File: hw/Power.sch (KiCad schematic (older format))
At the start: 32 parts, among them J201 Conn_01x02, Q201 AO3401A, Q202 AO3401A, Q203 IRLML6344TRPBF, Q204 IRLML6344TRPBF, U201 AP1501-K5, U202 RT6200

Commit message: Updates to board revision 0.2 and newer HAL version
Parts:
- removed Q201, Q202: AO3401A, digikey-footprints:SOT-23-3, symbol dk_Transistors-FETs-MOSFETs-Single:AO3401A
- removed Q203, Q204: IRLML6344TRPBF, digikey-footprints:SOT-23-3, symbol dk_Transistors-FETs-MOSFETs-Single:IRLML6344TRPBF
- removed R209, R210, R212, R214: 100k, Resistors_SMD:R_0603_HandSoldering, symbol Device:R_Small
- removed R211, R213: 10k, Resistors_SMD:R_0603_HandSoldering, symbol Device:R_Small
- U201: symbol Misc:AP1501-K5 -> Telemetry-rescue:AP1501-K5-Misc
- U202: symbol Misc:RT6200 -> Telemetry-rescue:RT6200-Misc
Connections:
- net labels removed: VBUS
- wire segments 114 -> 73

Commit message: Pin remapping and layout improvements
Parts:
- added C207, C212: 100n, Capacitor_SMD:C_0805_2012Metric_Pad1.15x1.40mm_HandSolder, symbol Device:C
- added C209, C210: 10n, Capacitor_SMD:C_0805_2012Metric_Pad1.15x1.40mm_HandSolder, symbol Device:C
- added C211: 100n, Capacitor_SMD:C_0805_2012Metric_Pad1.15x1.40mm_HandSolder, symbol Device:C_Small
- C201: value 22u -> 470uF/35V; footprint Capacitors_ThroughHole:C_Radial_D7.5_L11.2_P2.5 -> Capacitor_THT:CP_Radial_D10.0mm_P5.00mm
- C202, C208: value 22u -> 100uF/10V
- C203: footprint Capacitors_SMD:C_0603_HandSoldering -> Capacitor_SMD:C_0603_1608Metric_Pad1.05x0.95mm_HandSolder
- C205, C206: footprint Capacitors_SMD:C_0805 -> Capacitor_SMD:C_0805_2012Metric_Pad1.15x1.40mm_HandSolder
- R201: footprint Resistors_SMD:R_0603_HandSoldering -> Resistor_SMD:R_0603_1608Metric_Pad1.05x0.95mm_HandSolder; symbol Device:R -> Device:R_Small
- R202, R203, R204, R205, R206, R207, R208: footprint Resistors_SMD:R_0603_HandSoldering -> Resistor_SMD:R_0603_1608Metric_Pad1.05x0.95mm_HandSolder
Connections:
- net +BATT: now also C207.1, C209.1, C210.1; no longer R201.2
- net GND: now also R201.2, C207.2, C209.2, C212.2
- net VCC: now also C211.1, C212.1
- net at R202.2, R204.1, U201.4 (FB): now also C211.2
- net at R201.1, U201.5 (~SD): now also C210.2
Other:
- moved on the sheet: C202, C208, D202, L202, R201, R202, R204, U201

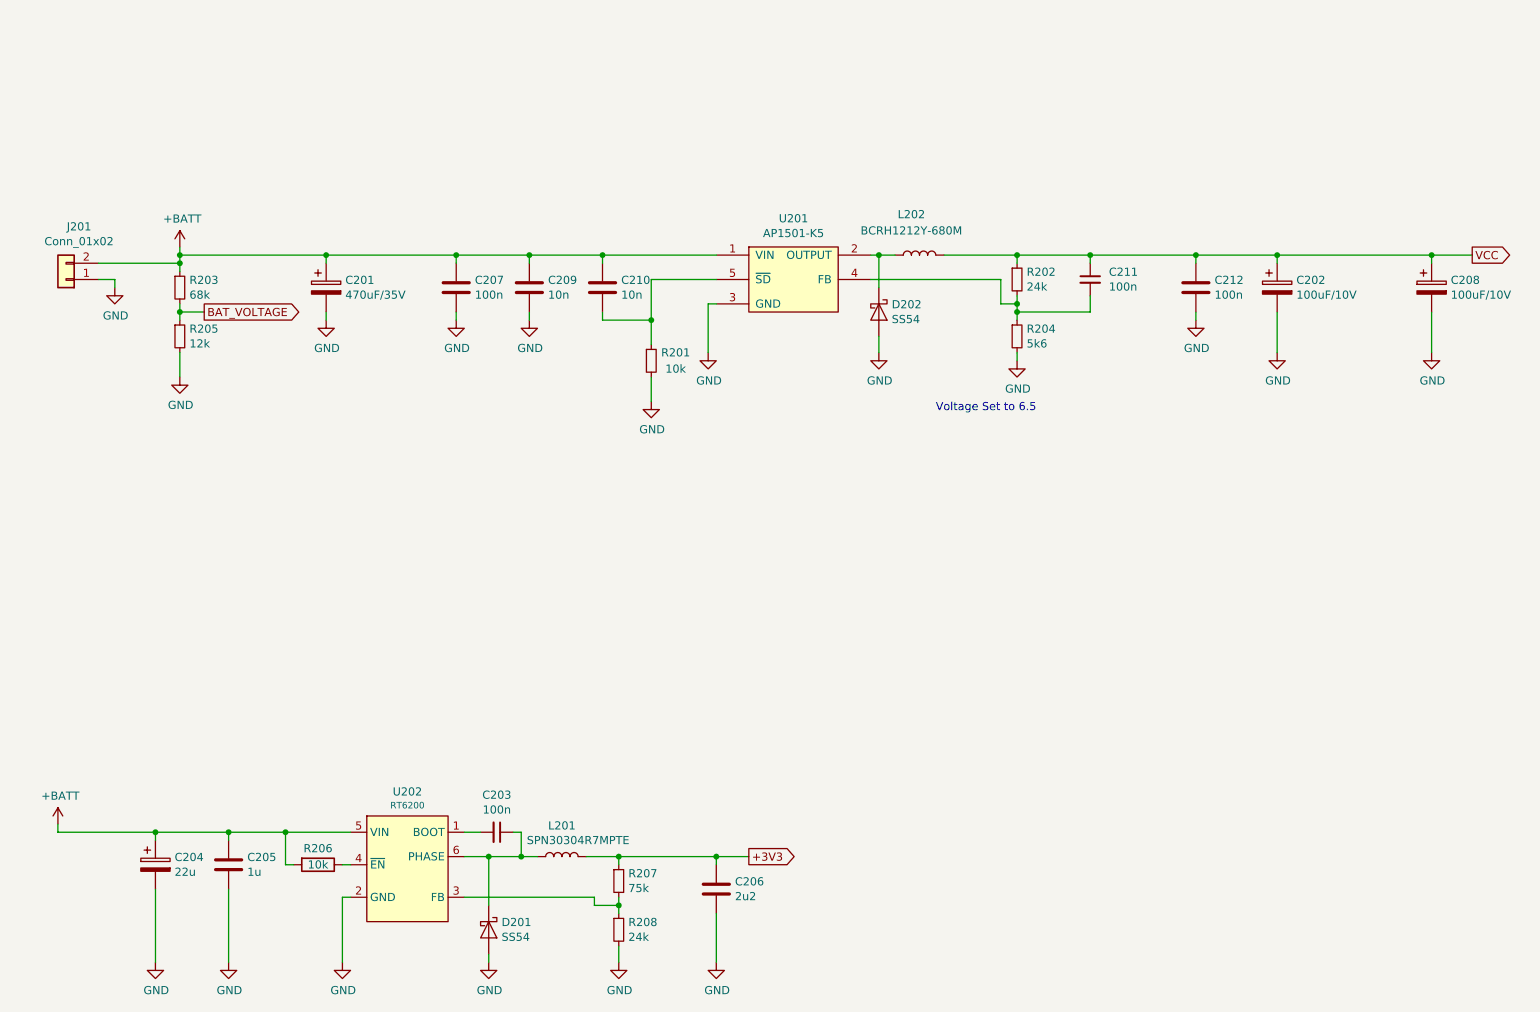
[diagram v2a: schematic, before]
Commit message: Changed High current pwm connectors to 5mm pitch versions
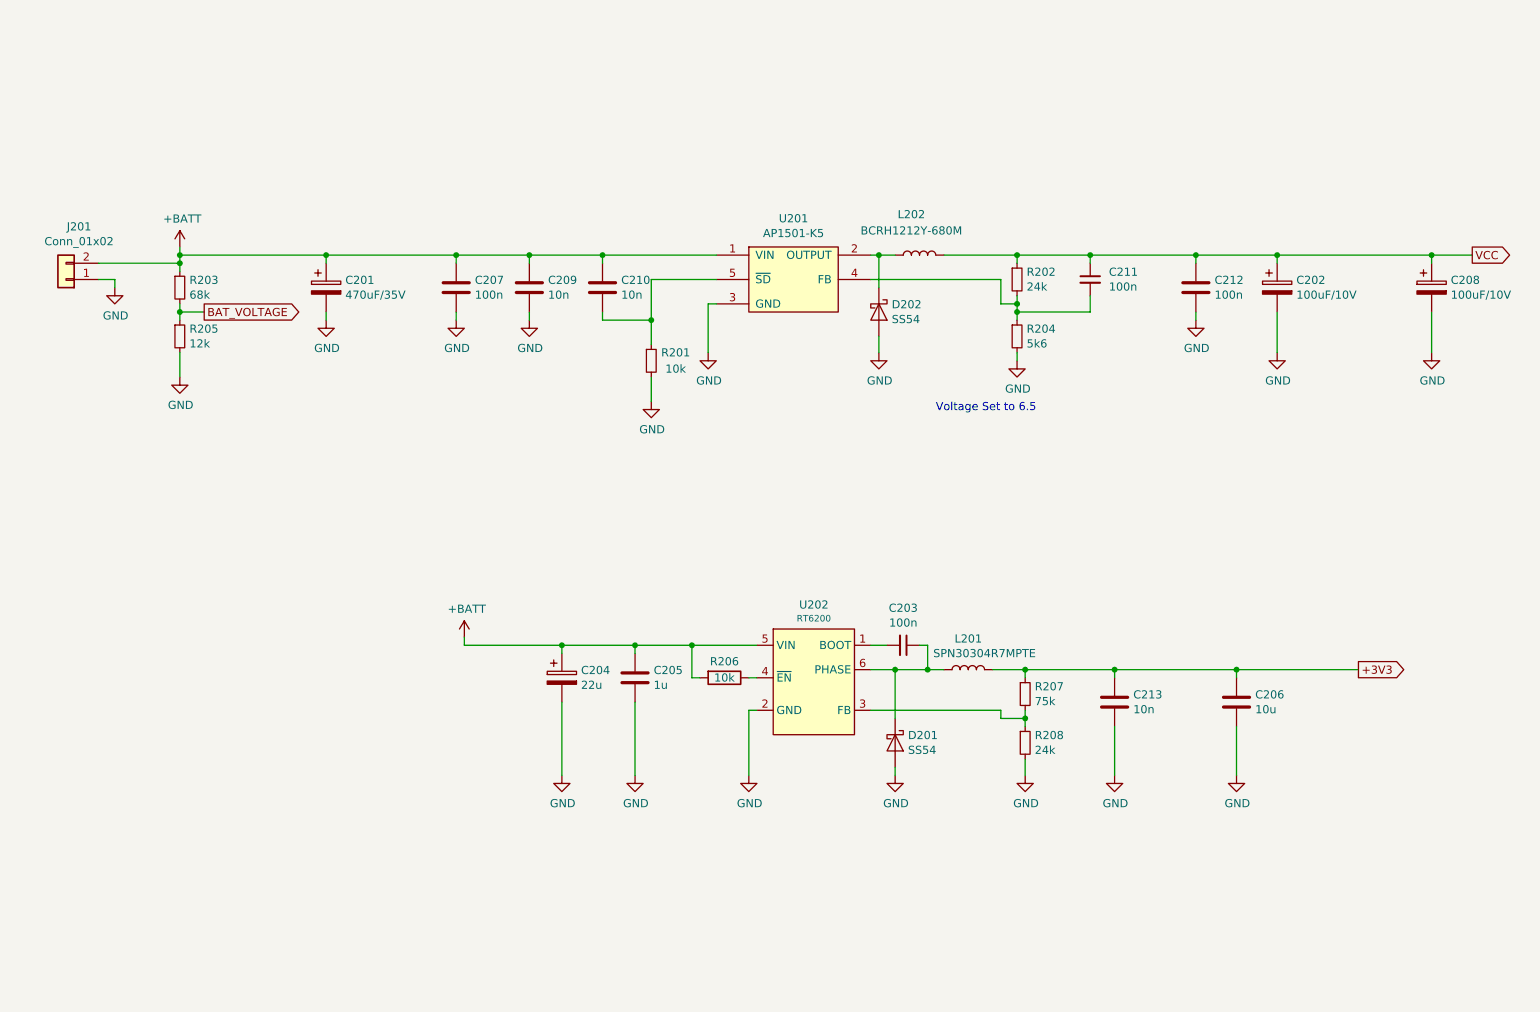
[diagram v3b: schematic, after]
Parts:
- added C213: 10n, Capacitor_SMD:C_0603_1608Metric_Pad1.05x0.95mm_HandSolder, symbol Device:C
- C206: value 2u2 -> 10u
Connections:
- net +3V3: now also C213.1
- net GND: now also C213.2
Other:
- moved on the sheet: C203, C204, C205, C206, D201, L201, R206, R207, R208, U202

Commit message: Added connector 3D model Changed inductors to be compatible with JLCPCB smt assembly
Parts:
- L201: footprint Inductors:Inductor_Taiyo-Yuden_MD-3030 -> PCBDecals:L_Sunlord_MWSA0402
- L202: footprint PCBDecals:12x12_inductor -> PCBDecals:L_Sunlord_MWSA1206
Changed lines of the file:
@@
 F 0 "L201" V 6740 4400 50  0000 C CNN
 F 1 " SPN30304R7MPTE" V 6650 4300 50  0000 C CNN
-F 2 "Inductors:Inductor_Taiyo-Yuden_MD-3030" H 6550 4400 50  0001 C CNN
+F 2 "PCBDecals:L_Sunlord_MWSA0402" H 6550 4400 50  0001 C CNN
 F 3 "https://datasheet.lcsc.com/szlcsc/1901081516_Darfon-Elec-SPN30304R7MPTE_C359291.pdf" H 6550 4400 50  0001 C CNN
 F 4 "C359291" V 6550 4400 50  0001 C CNN "LCSC Part-number"
@@
 F 0 "L202" V 6500 1900 50  0000 C CNN
 F 1 " BCRH1212Y-680M" V 6400 1900 50  0000 C CNN
-F 2 "PCBDecals:12x12_inductor" H 6250 1850 50  0001 C CNN
+F 2 "PCBDecals:L_Sunlord_MWSA1206" H 6250 1850 50  0001 C CNN
 F 3 "https://datasheet.lcsc.com/szlcsc/Bao-Cheng-Elec-BC-BCRH1212Y-680M_C238002.pdf" H 6250 1850 50  0001 C CNN
 F 4 " C238002" H 6250 1850 50  0001 C CNN "LCSC Part-number"

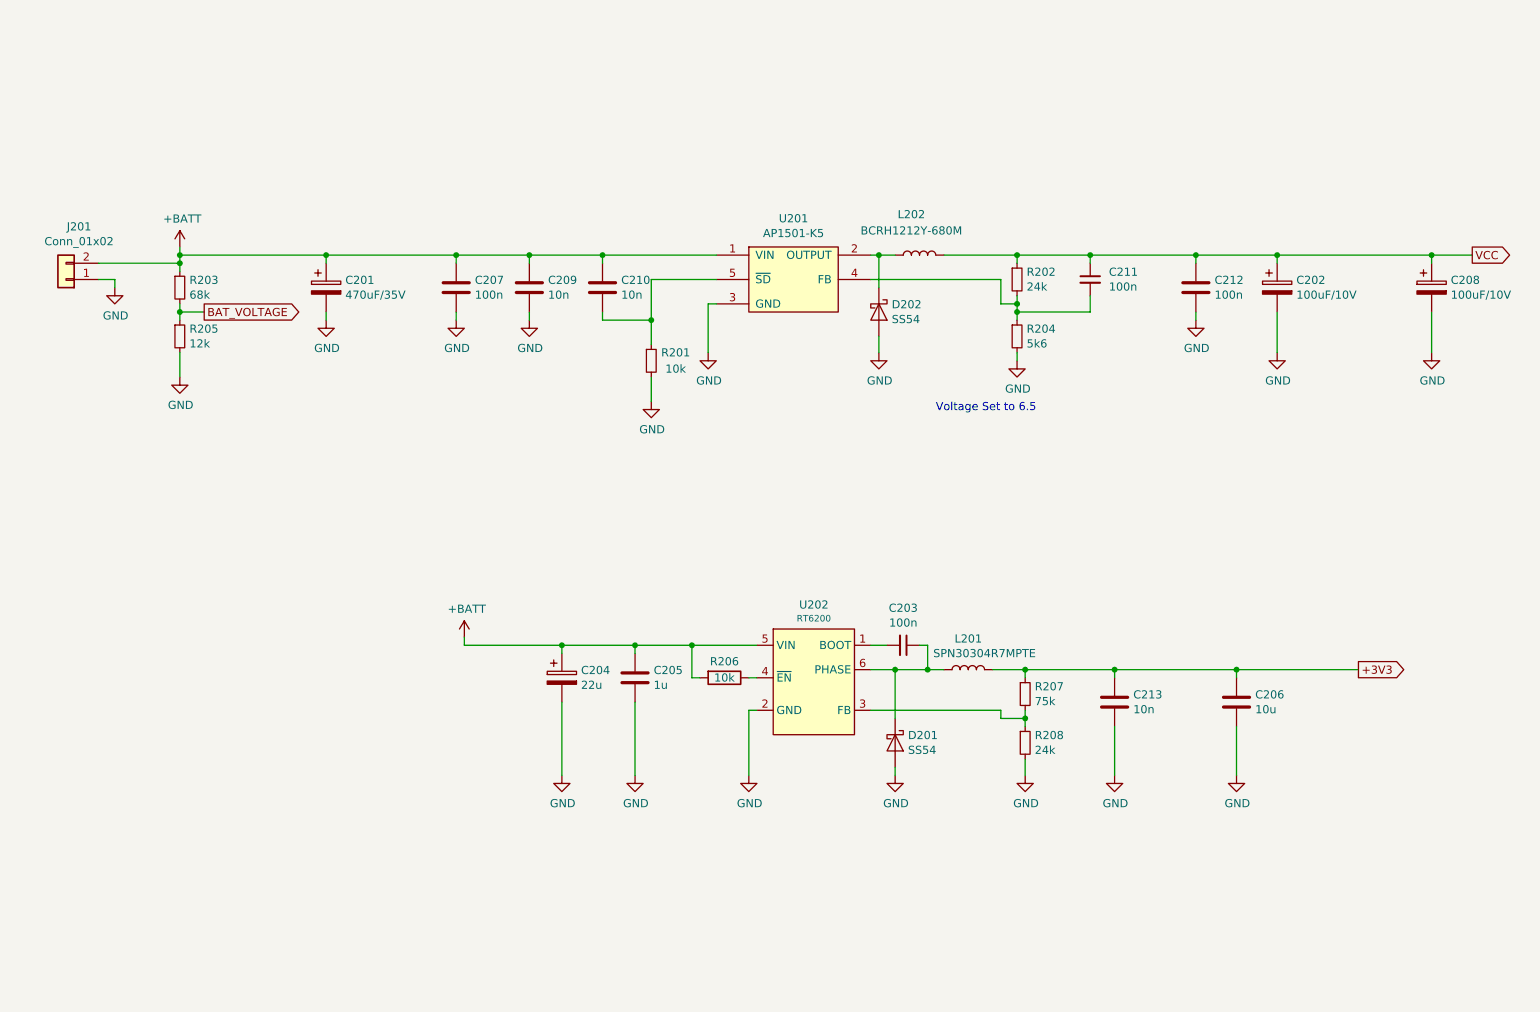
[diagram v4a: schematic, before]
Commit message: BOM Generation for 1.1 version
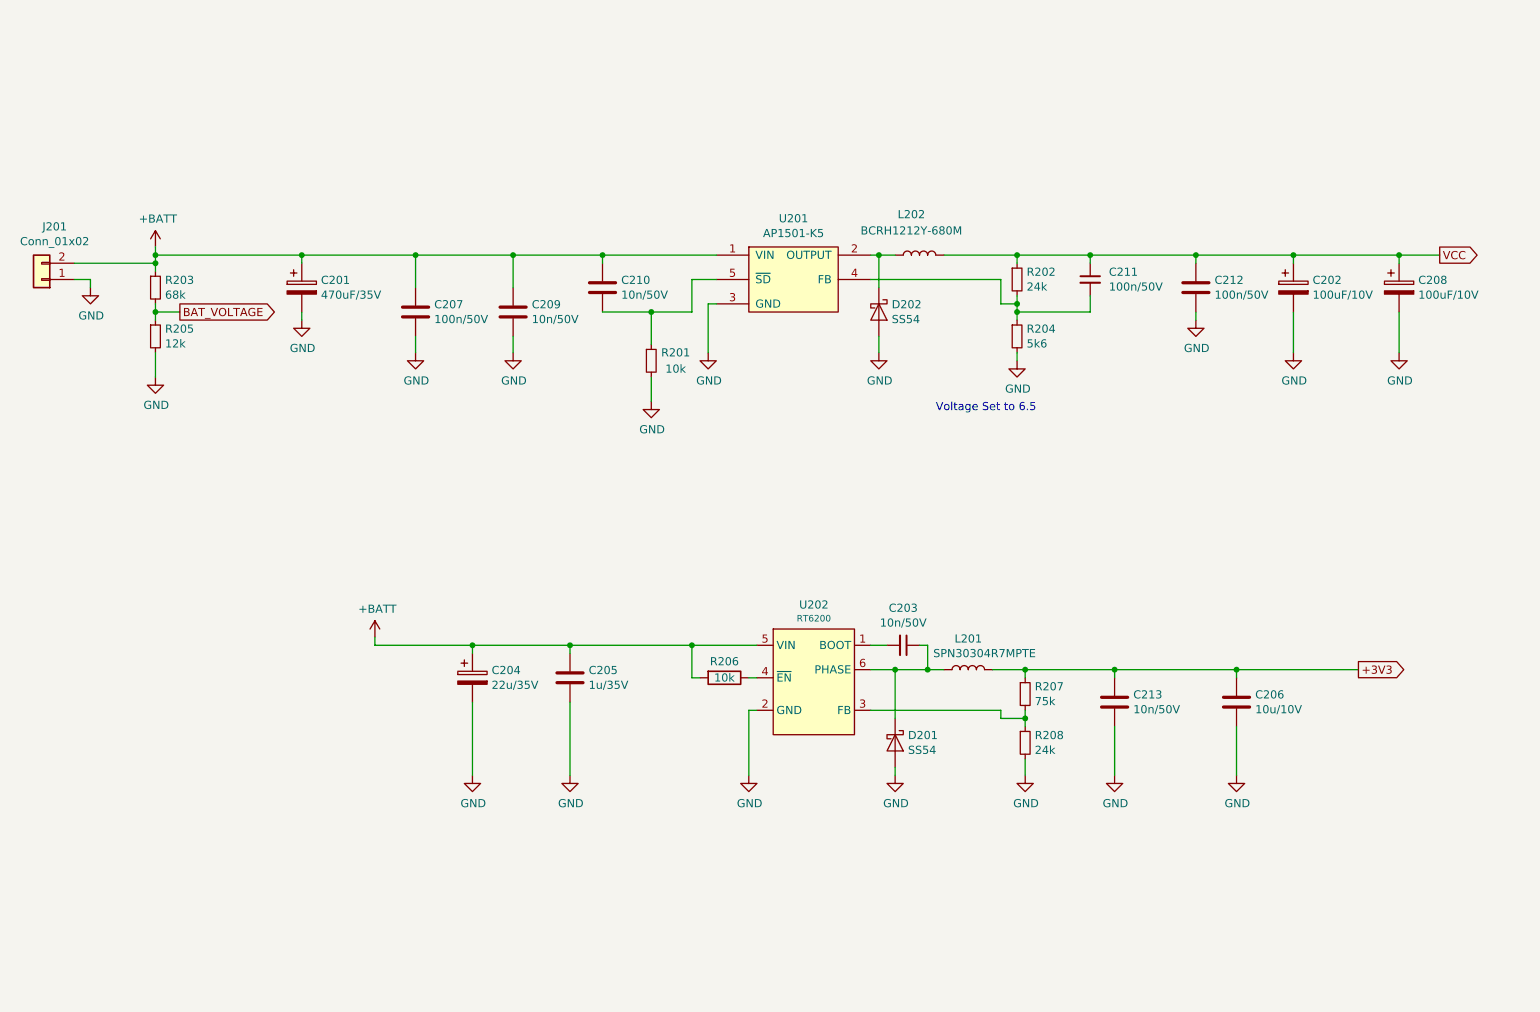
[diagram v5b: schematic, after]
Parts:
- C201, C202, C208, J201: Config (none) -> -prod
- C203: value 100n -> 10n/50V
- C204: value 22u -> 22u/35V; Config (none) -> -prod
- C205: value 1u -> 1u/35V
- C206: value 10u -> 10u/10V
- C207, C211, C212: value 100n -> 100n/50V
- C209, C210, C213: value 10n -> 10n/50V
- D201, D202: MPN (none) -> SS54
- L201: MPN (none) -> MWSA0402-4R7MT; Manufacturer (none) -> Sunlord
- L202: MPN (none) -> MWSA1206-470MT; Manufacturer (none) -> Sunlord
- U201: Description (none) -> 150kHz, 3A PWM Buck DC/DC Converter; MPN (none) -> AP1501-K5; Manufacturer (none) -> Diodes Inc
- U202: Description (none) -> 0.6A, 36V, 1.2MHz Step-Down Converter; MPN (none) -> RT6200; Manufacturer (none) -> Richtek Tech
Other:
- moved on the sheet: C201, C202, C204, C205, C207, C208, C209, J201, R203, R205

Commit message: Added additional opamp to DAC output as a buffer.
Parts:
- U202: footprint TO_SOT_Packages_SMD:SOT-23-6_Handsoldering -> Package_TO_SOT_SMD:SOT-23-6_Handsoldering
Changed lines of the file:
@@
 Sheet 2 4
 Title "RC Telemetry board"
-Date "2020-02-23"
+Date "2020-02-24"
 Rev "1.1"
 Comp "www.findersee.fi"
@@
 F 0 "U202" H 5600 4999 50  0000 C CNN
 F 1 "RT6200" H 5600 4915 40  0000 C CNN
-F 2 "TO_SOT_Packages_SMD:SOT-23-6_Handsoldering" H 5600 4500 50  0001 C CNN
+F 2 "Package_TO_SOT_SMD:SOT-23-6_Handsoldering" H 5600 4500 50  0001 C CNN
 F 3 "https://www.richtek.com/assets/product_file/RT6200/DS6200-04.pdf" H 5600 4500 50  0001 C CNN
 F 4 "RT6200" H 5600 4500 50  0001 C CNN "MPN"

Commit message: Signal remapping for Flash Memory and component optimizations
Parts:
- R204: value 5k6 -> 6k2
- U201: symbol Telemetry-rescue:AP1501-K5-Misc -> Telemetry-rescue:AP1501-K5-Misc-Telemetry-rescue
- U202: symbol Telemetry-rescue:RT6200-Misc -> Telemetry-rescue:RT6200-Misc-Telemetry-rescue
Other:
- note added: "Voltage Set to 6 V\n\n"
- note removed: "Voltage Set to 6.5\n\n"
- moved on the sheet: R201
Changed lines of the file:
@@
 $EndDescr
 $Comp
-L Telemetry-rescue:RT6200-Misc U202
+L Telemetry-rescue:RT6200-Misc-Telemetry-rescue U202
 U 1 1 5CE222A1
 P 5600 4500
+AR Path="/5CE222A1" Ref="U202"  Part="1"
+AR Path="/5CE22262/5CE222A1" Ref="U202"  Part="1"
 F 0 "U202" H 5600 4999 50  0000 C CNN
 F 1 "RT6200" H 5600 4915 40  0000 C CNN
@@
 P 6850 2350
 F 0 "R204" H 6909 2396 50  0000 L CNN
-F 1 "5k6" H 6909 2305 50  0000 L CNN
+F 1 "6k2" H 6909 2305 50  0000 L CNN
 F 2 "Resistor_SMD:R_0603_1608Metric_Pad1.05x0.95mm_HandSolder" H 6850 2350 50  0001 C CNN
 F 3 "~" H 6850 2350 50  0001 C CNN
@@
 	6100 5000 6100 5050
 Text Notes 6350 2900 0    50   ~ 0
-Voltage Set to 6.5\n\n
+Voltage Set to 6 V\n\n
 $Comp
 L Device:CP C201
@@
 	2900 4250 3500 4250
 $Comp
-L Telemetry-rescue:AP1501-K5-Misc U201
+L Telemetry-rescue:AP1501-K5-Misc-Telemetry-rescue U201
 U 1 1 5CE284E9
 P 5350 1950
+AR Path="/5CE284E9" Ref="U201"  Part="1"
+AR Path="/5CE22262/5CE284E9" Ref="U201"  Part="1"
 F 0 "U201" H 5475 2275 50  0000 C CNN
 F 1 "AP1501-K5" H 5475 2184 50  0000 C CNN
@@
 L Device:R_Small R201
 U 1 1 5CE2B122
-P 4600 2500
-F 0 "R201" H 4750 2550 50  0000 C CNN
-F 1 "10k" H 4750 2450 50  0000 C CNN
-F 2 "Resistor_SMD:R_0603_1608Metric_Pad1.05x0.95mm_HandSolder" V 4530 2500 50  0001 C CNN
-F 3 "~" H 4600 2500 50  0001 C CNN
-	1    4600 2500
+P 4300 2500
+F 0 "R201" H 4450 2550 50  0000 C CNN
+F 1 "10k" H 4450 2450 50  0000 C CNN
+F 2 "Resistor_SMD:R_0603_1608Metric_Pad1.05x0.95mm_HandSolder" V 4230 2500 50  0001 C CNN
+F 3 "~" H 4300 2500 50  0001 C CNN
+	1    4300 2500
 	1    0    0    -1
 $EndComp
@@
 L power:GND #PWR0215
 U 1 1 5E5D1E18
-P 4600 2750
-F 0 "#PWR0215" H 4600 2500 50  0001 C CNN
-F 1 "GND" H 4605 2577 50  0000 C CNN
-F 2 "" H 4600 2750 50  0001 C CNN
-F 3 "" H 4600 2750 50  0001 C CNN
-	1    4600 2750
-	1    0    0    -1
-$EndComp
-Wire Wire Line
-	4600 2600 4600 2750
+P 4300 2750
+F 0 "#PWR0215" H 4300 2500 50  0001 C CNN
+F 1 "GND" H 4305 2577 50  0000 C CNN
+F 2 "" H 4300 2750 50  0001 C CNN
+F 3 "" H 4300 2750 50  0001 C CNN
+	1    4300 2750
+	1    0    0    -1
+$EndComp
+Wire Wire Line
+	4300 2600 4300 2750
 $Comp
 L Device:C C210
@@
 $EndComp
 Wire Wire Line
-	4600 2200 4300 2200
-Connection ~ 4600 2200
-Wire Wire Line
-	4600 2200 4600 2400
+	4300 2250 4300 2200
+Connection ~ 4300 2250
+Wire Wire Line
+	4300 2250 4300 2400
 Wire Wire Line
 	4300 1900 4300 1850
@@
 	7450 4750 7450 5050
 Wire Wire Line
-	4600 2200 4850 2200
-Wire Wire Line
-	4850 2200 4850 2000
+	4300 2250 4850 2250
+Wire Wire Line
+	4850 2250 4850 2000
 Wire Wire Line
 	4850 2000 5000 2000
